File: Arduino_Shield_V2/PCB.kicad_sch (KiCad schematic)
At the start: 14 parts, among them IC1 LTC6090HFE#PBF, J1 Power, J2 Digital/PWM, J3 Analog, J4 Digital/PWM, J6 Conn_01x01_Socket, U4 MCP4921

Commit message: Serious edits during 2/22 meeting by Eric
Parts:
- removed IC1: LTC6090HFE#PBF, SOP65P640X110-17N, symbol LTC6090HFE#PBF:LTC6090HFE#PBF
- added C3, C4: 0.1uF, Capacitor_SMD:C_1206_3216Metric_Pad1.33x1.80mm_HandSolder, symbol Device:C
- added J5, J7, J8: Conn_01x01, Connector_Pin:Pin_D1.0mm_L10.0mm, symbol Connector_Generic:Conn_01x01
- added U2: LTC6090, Package_SO:SOIC-8-1EP_3.9x4.9mm_P1.27mm_EP2.29x3mm, symbol my_opamp:LTC6090
- R1, R2, R3, R4, R6: footprint Resistor_THT:R_Axial_DIN0309_L9.0mm_D3.2mm_P12.70mm_Horizontal -> Resistor_SMD:R_1206_3216Metric_Pad1.30x1.75mm_HandSolder
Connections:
- net GND: now also C3.2, C4.2, J8.1 (Pin_1)
- net SCL/A5: no longer J2.1 (Pin_1)
- net SDA/A4: no longer J2.2 (Pin_2)
- net at C1.1, R1.2: now also U2.3
- net at C2.1, R2.1, R3.2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: now also U2.2
- net at C2.2, R4.2, R6.1: now also U2.6
- new net -VSW: C4.1, J7.1 (Pin_1), U2.4
- new net HT: C3.1, J5.1 (Pin_1), U2.7

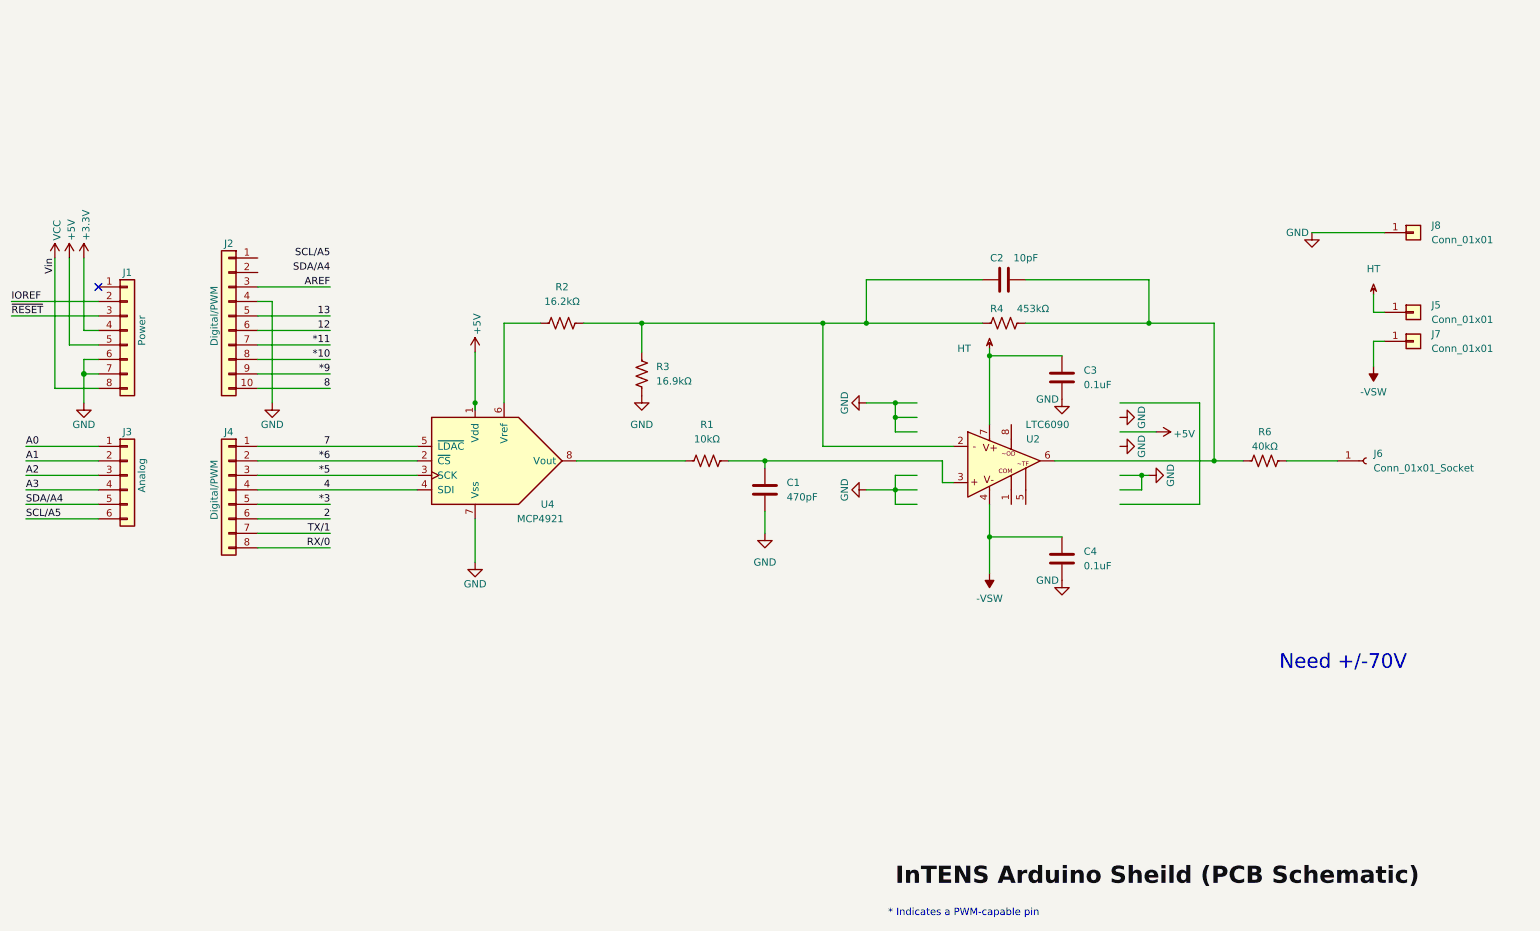
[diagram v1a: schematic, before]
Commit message: fixed scematic wiring, PCB tracks, checked footprint dimensions, and added 3D models
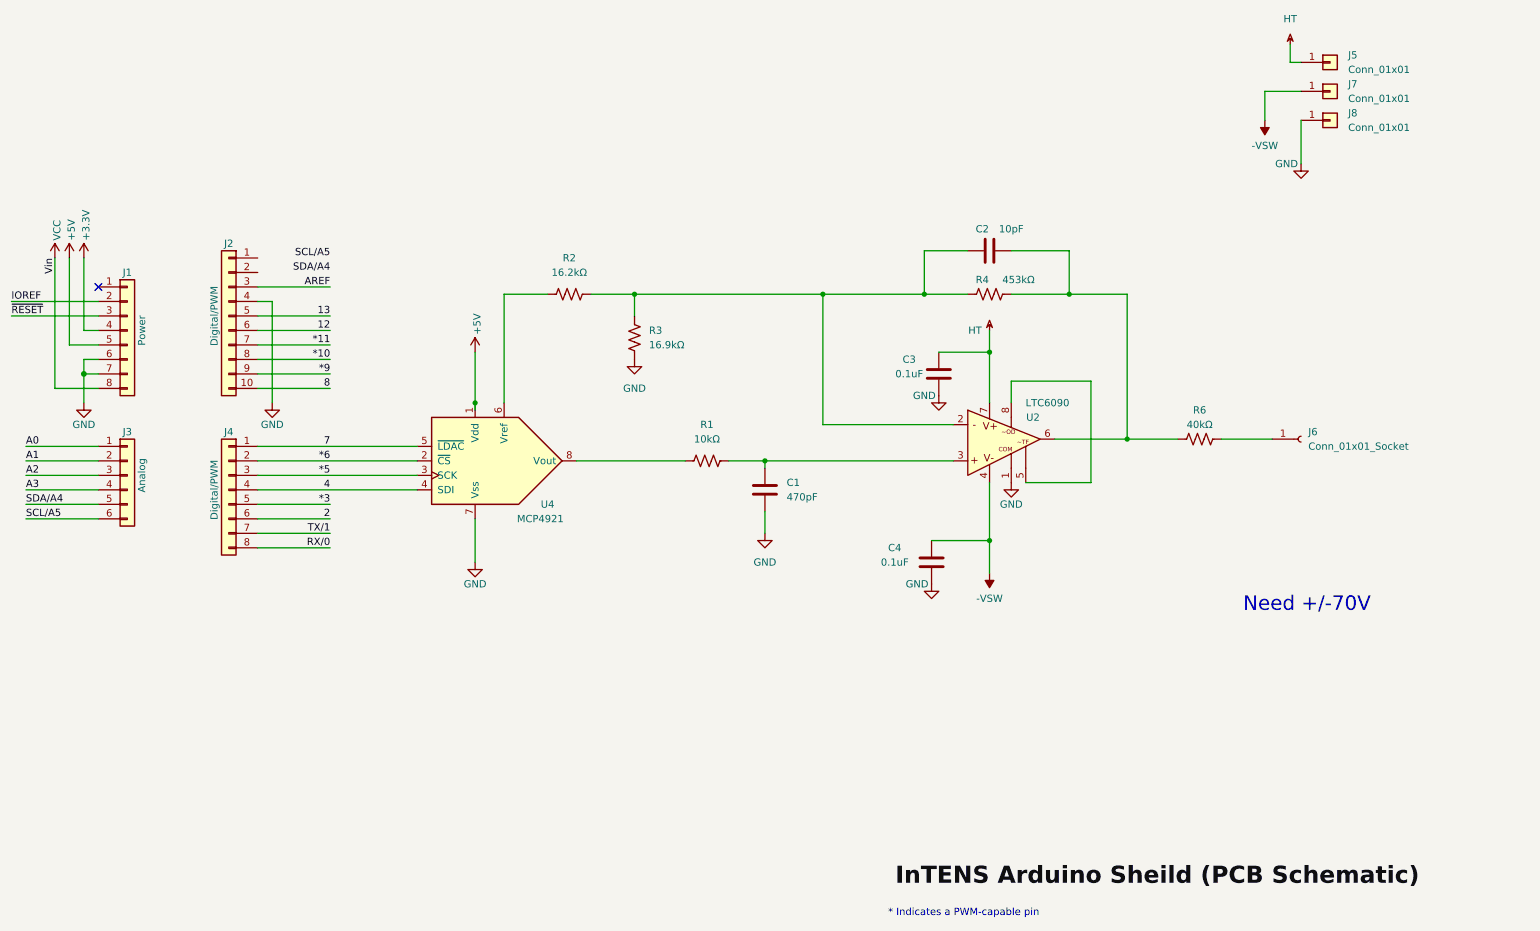
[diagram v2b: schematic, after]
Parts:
- C1, C2: footprint Capacitor_THT:C_Axial_L3.8mm_D2.6mm_P12.50mm_Horizontal -> Capacitor_SMD:C_1206_3216Metric_Pad1.33x1.80mm_HandSolder
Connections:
- net GND: now also U2.1
- net at U2.5: now also U2.8
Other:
- moved on the sheet: C2, C3, C4, J5, J6, J7, J8, R2, R3, R4, R6, U2

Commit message: semi-updated from Eric 3/4 notes
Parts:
- added C5: 0.1 uF, Capacitor_SMD:C_1206_3216Metric_Pad1.33x1.80mm_HandSolder, symbol Device:C
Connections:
- net +5V: now also C5.1
- net GND: now also C5.2
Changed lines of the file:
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@@
   (junction (at 105.41 90.17) (diameter 0) (color 0 0 0 0)
+  )
+  (junction (at 105.41 77.47) (diameter 0) (color 0 0 0 0)
   )
   (junction (at 209.55 71.12) (diameter 0) (color 0 0 0 0)
@@
     (stroke (width 0) (type default))
   )
-  (wire (pts (xy 105.41 81.28) (xy 105.41 90.17))
+  (wire (pts (xy 105.41 69.85) (xy 105.41 77.47))
     (stroke (width 0) (type default))
   )
@@
     (stroke (width 0) (type solid))
   )
+  (wire (pts (xy 96.52 77.47) (xy 105.41 77.47))
+    (stroke (width 0) (type default))
+  )
   (wire (pts (xy 67.31 97.79) (xy 95.25 97.79))
     (stroke (width 0) (type default))
@@
   )
   (wire (pts (xy 67.31 105.41) (xy 95.25 105.41))
+    (stroke (width 0) (type default))
+  )
+  (wire (pts (xy 105.41 77.47) (xy 105.41 90.17))
     (stroke (width 0) (type default))
   )
@@
     )
   )
-  (symbol (lib_id "power:+5V") (at 105.41 81.28 0) (unit 1)
-    (in_bom yes) (on_board yes) (dnp no)
-    (property "Reference" "#PWR07" (at 105.41 85.09 0)
-      (effects (font (size 1.27 1.27)) hide)
-    )
-    (property "Value" "+5V" (at 105.7656 78.232 90)
-      (effects (font (size 1.27 1.27)) (justify left))
-    )
-    (property "Footprint" "" (at 105.41 81.28 0)
-      (effects (font (size 1.27 1.27)))
-    )
-    (property "Datasheet" "" (at 105.41 81.28 0)
+  (symbol (lib_id "power:+5V") (at 105.41 69.85 0) (unit 1)
+    (in_bom yes) (on_board yes) (dnp no)
+    (property "Reference" "#PWR07" (at 105.41 73.66 0)
+      (effects (font (size 1.27 1.27)) hide)
+    )
+    (property "Value" "+5V" (at 105.7656 66.802 90)
+      (effects (font (size 1.27 1.27)) (justify left))
+    )
+    (property "Footprint" "" (at 105.41 69.85 0)
+      (effects (font (size 1.27 1.27)))
+    )
+    (property "Datasheet" "" (at 105.41 69.85 0)
       (effects (font (size 1.27 1.27)))
     )
@@
     )
   )
+  (symbol (lib_id "Device:C") (at 96.52 81.28 0) (unit 1)
+    (in_bom yes) (on_board yes) (dnp no) (fields_autoplaced)
+    (property "Reference" "C5" (at 100.33 80.01 0)
+      (effects (font (size 1.27 1.27)) (justify left))
+    )
+    (property "Value" "0.1 uF" (at 100.33 82.55 0)
+      (effects (font (size 1.27 1.27)) (justify left))
+    )
+    (property "Footprint" "Capacitor_SMD:C_1206_3216Metric_Pad1.33x1.80mm_HandSolder" (at 97.4852 85.09 0)
+      (effects (font (size 1.27 1.27)) hide)
+    )
+    (property "Datasheet" "~" (at 96.52 81.28 0)
+      (effects (font (size 1.27 1.27)) hide)
+    )
+    (pin "2")
+    (pin "1")
+    (instances
+      (project "PCB"
+        (path "/e63e39d7-6ac0-4ffd-8aa3-1841a4541b55"
+          (reference "C5") (unit 1)
+        )
+      )
+    )
+  )
   (symbol (lib_id "power:VCC") (at 31.75 64.77 0) (unit 1)
     (in_bom yes) (on_board yes) (dnp no)
@@
   )
   (symbol (lib_id "power:-VSW") (at 243.84 40.64 180) (unit 1)
-    (in_bom yes) (on_board yes) (dnp no) (fields_autoplaced)
+    (in_bom yes) (on_board yes) (dnp no)
     (property "Reference" "#PWR020" (at 243.84 43.18 0)
       (effects (font (size 1.27 1.27)) hide)
@@
   )
   (symbol (lib_id "power:HT") (at 248.285 27.305 0) (unit 1)
-    (in_bom yes) (on_board yes) (dnp no) (fields_autoplaced)
+    (in_bom yes) (on_board yes) (dnp no)
     (property "Reference" "#PWR018" (at 248.285 24.257 0)
       (effects (font (size 1.27 1.27)) hide)
@@
         )
       )
+    )
+  )
+  (symbol (lib_id "power:GND") (at 96.52 85.09 0) (unit 1)
+    (in_bom yes) (on_board yes) (dnp no)
+    (property "Reference" "#PWR011" (at 96.52 91.44 0)
+      (effects (font (size 1.27 1.27)) hide)
+    )
+    (property "Value" "GND" (at 96.52 88.9 0)
+      (effects (font (size 1.27 1.27)))
+    )
+    (property "Footprint" "" (at 96.52 85.09 0)
+      (effects (font (size 1.27 1.27)))
+    )
+    (property "Datasheet" "" (at 96.52 85.09 0)
+      (effects (font (size 1.27 1.27)))
+    )
+    (pin "1")
+    (instances
+      (project "PCB"
+        (path "/e63e39d7-6ac0-4ffd-8aa3-1841a4541b55"
+          (reference "#PWR011") (unit 1)
+        )
+      )

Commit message: updated PCB from 3/4 Eric Meeting
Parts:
- J6: symbol Connector:Conn_01x01_Socket -> Connector:Conn_01x02_Socket
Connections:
- net GND: now also J6.2 (Pin_2)
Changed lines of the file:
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@@
     (stroke (width 0) (type solid))
+  )
+  (wire (pts (xy 245.11 99.06) (xy 243.84 99.06))
+    (stroke (width 0) (type default))
   )
   (wire (pts (xy 39.37 82.55) (xy 36.83 82.55))
@@
   )
   (wire (pts (xy 248.285 30.48) (xy 250.19 30.48))
+    (stroke (width 0) (type default))
+  )
+  (wire (pts (xy 243.84 99.06) (xy 243.84 102.87))
     (stroke (width 0) (type default))
   )
@@
     )
   )
+  (symbol (lib_id "power:GND") (at 243.84 102.87 0) (unit 1)
+    (in_bom yes) (on_board yes) (dnp no)
+    (property "Reference" "#PWR012" (at 243.84 109.22 0)
+      (effects (font (size 1.27 1.27)) hide)
+    )
+    (property "Value" "GND" (at 241.3 102.87 0)
+      (effects (font (size 1.27 1.27)))
+    )
+    (property "Footprint" "" (at 243.84 102.87 0)
+      (effects (font (size 1.27 1.27)))
+    )
+    (property "Datasheet" "" (at 243.84 102.87 0)
+      (effects (font (size 1.27 1.27)))
+    )
+    (pin "1")
+    (instances
+      (project "PCB"
+        (path "/e63e39d7-6ac0-4ffd-8aa3-1841a4541b55"
+          (reference "#PWR012") (unit 1)
+        )
+      )
+    )
+  )
   (symbol (lib_id "power:VCC") (at 31.75 64.77 0) (unit 1)
     (in_bom yes) (on_board yes) (dnp no)
@@
     )
   )
-  (symbol (lib_id "Connector:Conn_01x01_Socket") (at 250.19 96.52 0) (unit 1)
+  (symbol (lib_id "Connector:Conn_01x02_Socket") (at 250.19 96.52 0) (unit 1)
     (in_bom yes) (on_board yes) (dnp no) (fields_autoplaced)
-    (property "Reference" "J6" (at 251.46 95.25 0)
-      (effects (font (size 1.27 1.27)) (justify left))
-    )
-    (property "Value" "Conn_01x01_Socket" (at 251.46 97.79 0)
+    (property "Reference" "J6" (at 251.46 96.52 0)
+      (effects (font (size 1.27 1.27)) (justify left))
+    )
+    (property "Value" "Conn_01x01_Socket" (at 251.46 99.06 0)
       (effects (font (size 1.27 1.27)) (justify left))
     )
@@
     )
     (pin "1")
-    (instances
-      (project "PCB"
+    (pin "2")
+    (instances
+      (project "PCB"

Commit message: ERIC:  Add part numbers to symbols for ordering
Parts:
- added N1: Breakaway_header_for_Arduino, symbol Mechanical:Housing
- C1: CatNo (none) -> 732-8100-1-ND; MfgNo (none) -> 885012208044
- C2: CatNo (none) -> 4713-GMC31CG100J100NTCT-ND; MfgNo (none) -> GMC31CG100J100NT
- C3, C4: CatNo (none) -> 1276-1151-1-ND; MfgNo (none) -> CL31B104KCFNNNE
- C5: value 0.1 uF -> 0.1uF; CatNo (none) -> 1276-1151-1-ND; MfgNo (none) -> CL31B104KCFNNNE
- J1, J2, J3, J4: now left out of the parts list
- R1: CatNo (none) -> 311-10.0KFRCT-ND; MfgNo (none) -> RC1206FR-0710KL
- R2: CatNo (none) -> 311-16.2KFRCT-ND; MfgNo (none) -> RC1206FR-0716K2L
- R3: CatNo (none) -> 311-16.9KFRCT-ND; MfgNo (none) -> RC1206FR-0716K9L
- R4: CatNo (none) -> 311-453KFRCT-ND; MfgNo (none) -> RC1206FR-07453KL
- R6: value 40kΩ -> 40.2k; CatNo (none) -> 311-40.2KFRCT-ND; MfgNo (none) -> RC1206FR-0740K2L
- U2: CatNo (none) -> 505-LTC6090CS8E-5#PBF-ND; MfgNo (none) -> LTC6090CS8E-5#PBF
- U4: CatNo (none) -> MCP4921-E/P-ND; MfgNo (none) -> MCP4921-E/P
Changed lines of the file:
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@@
   )
   (symbol (lib_id "Connector_Generic:Conn_01x08") (at 44.45 77.47 0) (unit 1)
-    (in_bom yes) (on_board yes) (dnp no)
+    (in_bom no) (on_board yes) (dnp no)
     (property "Reference" "J1" (at 44.45 67.31 0)
       (effects (font (size 1.27 1.27)))
@@
   )
   (symbol (lib_id "Connector_Generic:Conn_01x10") (at 62.23 74.93 0) (mirror y) (unit 1)
-    (in_bom yes) (on_board yes) (dnp no)
+    (in_bom no) (on_board yes) (dnp no)
     (property "Reference" "J2" (at 62.23 62.23 0)
       (effects (font (size 1.27 1.27)))
@@
   )
   (symbol (lib_id "Connector_Generic:Conn_01x06") (at 44.45 102.87 0) (unit 1)
-    (in_bom yes) (on_board yes) (dnp no)
+    (in_bom no) (on_board yes) (dnp no)
     (property "Reference" "J3" (at 44.45 95.25 0)
       (effects (font (size 1.27 1.27)))
@@
   )
   (symbol (lib_id "Connector_Generic:Conn_01x08") (at 62.23 105.41 0) (mirror y) (unit 1)
-    (in_bom yes) (on_board yes) (dnp no)
+    (in_bom no) (on_board yes) (dnp no)
     (property "Reference" "J4" (at 62.23 95.25 0)
       (effects (font (size 1.27 1.27)))
@@
   )
   (symbol (lib_id "Device:C") (at 156.21 105.41 0) (unit 1)
-    (in_bom yes) (on_board yes) (dnp no) (fields_autoplaced)
+    (in_bom yes) (on_board yes) (dnp no)
     (property "Reference" "C1" (at 160.02 104.14 0)
       (effects (font (size 1.27 1.27)) (justify left))
@@
     )
     (property "Datasheet" "~" (at 156.21 105.41 0)
+      (effects (font (size 1.27 1.27)) hide)
+    )
+    (property "CatNo" "732-8100-1-ND" (at 167.64 109.22 0)
+      (effects (font (size 1.27 1.27)))
+    )
+    (property "MfgNo" "885012208044" (at 156.21 105.41 0)
       (effects (font (size 1.27 1.27)) hide)
     )
@@
       (effects (font (size 1.27 1.27)) (justify left))
     )
-    (property "Value" "0.1 uF" (at 100.33 82.55 0)
+    (property "Value" "0.1uF" (at 100.33 82.55 0)
       (effects (font (size 1.27 1.27)) (justify left))
     )
@@
     )
     (property "Datasheet" "~" (at 96.52 81.28 0)
+      (effects (font (size 1.27 1.27)) hide)
+    )
+    (property "CatNo" "1276-1151-1-ND" (at 96.52 81.28 0)
+      (effects (font (size 1.27 1.27)) hide)
+    )
+    (property "MfgNo" "CL31B104KCFNNNE" (at 96.52 81.28 0)
       (effects (font (size 1.27 1.27)) hide)
     )
@@
       (effects (font (size 1.27 1.27)) hide)
     )
+    (property "CatNo" "311-453KFRCT-ND" (at 195.58 71.12 0)
+      (effects (font (size 1.27 1.27)) hide)
+    )
+    (property "MfgNo" "RC1206FR-07453KL" (at 195.58 71.12 0)
+      (effects (font (size 1.27 1.27)) hide)
+    )
     (pin "1")
     (pin "2")
@@
       (effects (font (size 1.27 1.27)) hide)
     )
+    (property "CatNo" "311-16.2KFRCT-ND" (at 121.92 71.12 0)
+      (effects (font (size 1.27 1.27)) hide)
+    )
+    (property "MfgNo" "RC1206FR-0716K2L" (at 121.92 71.12 0)
+      (effects (font (size 1.27 1.27)) hide)
+    )
     (pin "1")
     (pin "2")
@@
     )
     (property "Datasheet" "" (at 189.23 93.98 0)
+      (effects (font (size 1.27 1.27)) hide)
+    )
+    (property "CatNo" "505-LTC6090CS8E-5#PBF-ND" (at 189.23 93.98 0)
+      (effects (font (size 1.27 1.27)) hide)
+    )
+    (property "MfgNo" "LTC6090CS8E-5#PBF" (at 189.23 93.98 0)
       (effects (font (size 1.27 1.27)) hide)
     )
@@
       (effects (font (size 1.27 1.27)) hide)
     )
+    (property "CatNo" "1276-1151-1-ND" (at 186.69 85.09 0)
+      (effects (font (size 1.27 1.27)) hide)
+    )
+    (property "MfgNo" "CL31B104KCFNNNE" (at 186.69 85.09 0)
+      (effects (font (size 1.27 1.27)) hide)
+    )
     (pin "1")
     (pin "2")
@@
       (effects (font (size 1.27 1.27)) hide)
     )
+    (property "CatNo" "1276-1151-1-ND" (at 185.42 118.11 0)
+      (effects (font (size 1.27 1.27)) hide)
+    )
+    (property "MfgNo" "CL31B104KCFNNNE" (at 185.42 118.11 0)
+      (effects (font (size 1.27 1.27)) hide)
+    )
     (pin "1")
     (pin "2")
@@
     )
     (property "Datasheet" "~" (at 195.58 63.5 0)
+      (effects (font (size 1.27 1.27)) hide)
+    )
+    (property "CatNo" "4713-GMC31CG100J100NTCT-ND" (at 195.58 63.5 0)
+      (effects (font (size 1.27 1.27)) hide)
+    )
+    (property "MfgNo" "GMC31CG100J100NT" (at 195.58 63.5 0)
       (effects (font (size 1.27 1.27)) hide)
     )
@@
       (effects (font (size 1.27 1.27)))
     )
-    (property "Value" "40kΩ" (at 232.41 93.98 90)
+    (property "Value" "40.2k" (at 232.41 93.98 90)
       (effects (font (size 1.27 1.27)))
     )
@@
     )
     (property "Datasheet" "~" (at 232.41 96.52 0)
+      (effects (font (size 1.27 1.27)) hide)
+    )
+    (property "CatNo" "311-40.2KFRCT-ND" (at 232.41 96.52 0)
+      (effects (font (size 1.27 1.27)) hide)
+    )
+    (property "MfgNo" "RC1206FR-0740K2L" (at 232.41 96.52 0)
       (effects (font (size 1.27 1.27)) hide)
     )
@@
     )
     (property "Datasheet" "http://ww1.microchip.com/downloads/en/DeviceDoc/22248a.pdf" (at 130.81 102.87 0)
+      (effects (font (size 1.27 1.27)) hide)
+    )
+    (property "CatNo" "MCP4921-E/P-ND" (at 105.41 100.33 0)
+      (effects (font (size 1.27 1.27)) hide)
+    )
+    (property "MfgNo" "MCP4921-E/P" (at 105.41 100.33 0)
       (effects (font (size 1.27 1.27)) hide)
     )
@@
       (effects (font (size 1.27 1.27)) hide)
     )
+    (property "CatNo" "311-16.9KFRCT-ND" (at 133.35 78.74 0)
+      (effects (font (size 1.27 1.27)) hide)
+    )
+    (property "MfgNo" "RC1206FR-0716K9L" (at 133.35 78.74 0)
+      (effects (font (size 1.27 1.27)) hide)
+    )
     (pin "1")
     (pin "2")
@@
       (effects (font (size 1.27 1.27)) hide)
     )
+    (property "CatNo" "311-10.0KFRCT-ND" (at 146.05 100.33 0)
+      (effects (font (size 1.27 1.27)) hide)
+    )
+    (property "MfgNo" "RC1206FR-0710KL" (at 146.05 100.33 0)
+      (effects (font (size 1.27 1.27)) hide)
+    )
     (pin "1")
     (pin "2")
@@
         )
       )
+    )
+  )
+  (symbol (lib_id "Mechanical:Housing") (at 47.625 132.715 0) (unit 1)
+    (in_bom yes) (on_board yes) (dnp no) (fields_autoplaced)
+    (property "Reference" "N1" (at 52.07 131.7625 0)
+      (effects (font (size 1.27 1.27)) (justify left))
+    )
+    (property "Value" "Breakaway_header_for_Arduino" (at 52.07 134.3025 0)
+      (effects (font (size 1.27 1.27)) (justify left))
+    )
+    (property "Footprint" "" (at 48.895 131.445 0)
+      (effects (font (size 1.27 1.27)) hide)
+    )
+    (property "Datasheet" "~" (at 48.895 131.445 0)
+      (effects (font (size 1.27 1.27)) hide)
+    )
+    (property "CatNo" "952-3307-ND" (at 47.625 132.715 0)
+      (effects (font (size 1.27 1.27)) hide)
+    )
+    (property "MfgNo" "M20-9994045" (at 47.625 132.715 0)
+      (effects (font (size 1.27 1.27)) hide)
+    )
+    (instances
+      (project "PCB"
+        (path "/e63e39d7-6ac0-4ffd-8aa3-1841a4541b55"
+          (reference "N1") (unit 1)
+        )
+      )
